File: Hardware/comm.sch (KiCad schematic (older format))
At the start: 13 parts, among them P301 PROGRAM, P302 OUTPUT, P303 INPUT, P304 BOOT, SW301 SW_Push

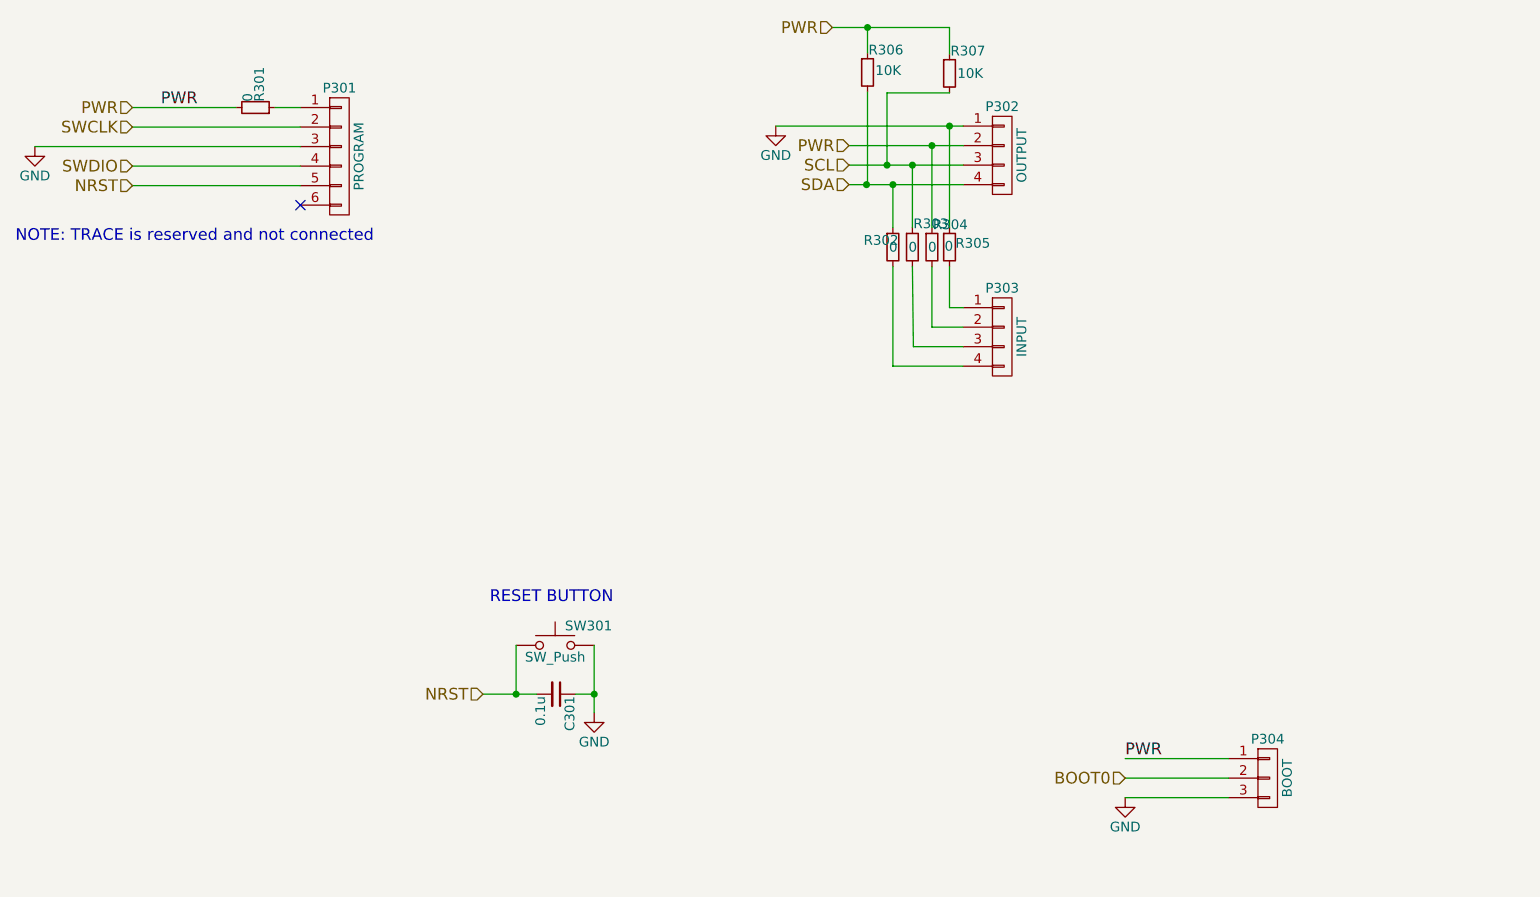
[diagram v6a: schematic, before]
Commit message: converted VCCIO to 3V3 and added 1x2 power and gnd
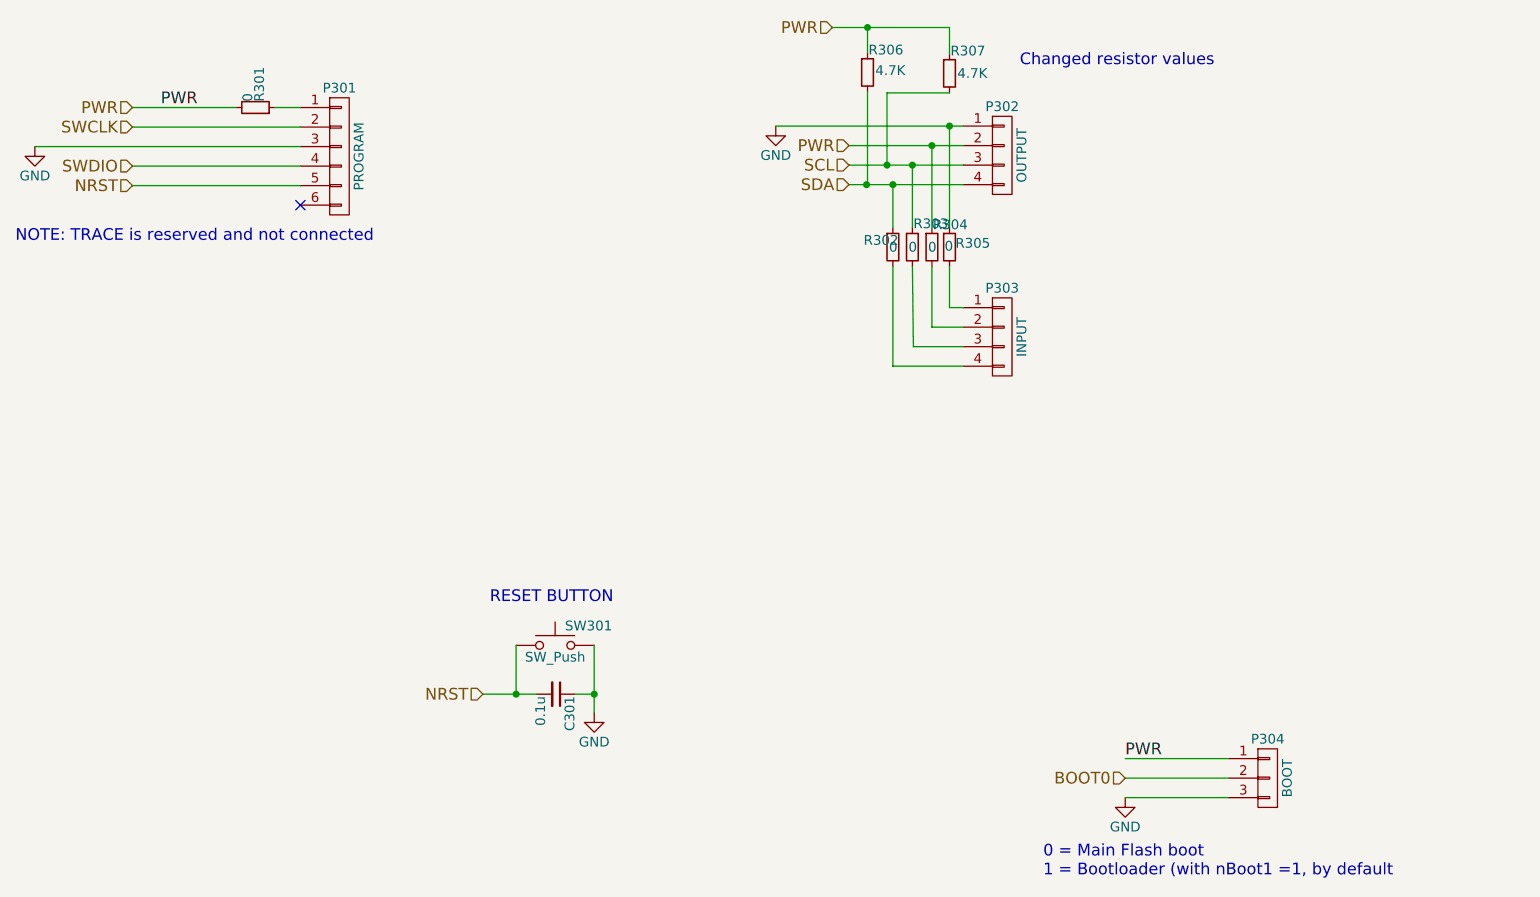
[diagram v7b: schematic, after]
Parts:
- R306, R307: value 10K -> 4.7K
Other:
- note added: "0 = Main Flash boot\n1 = Bootloader (with nBoot1 =1, by default"
- note added: "Changed resistor values"
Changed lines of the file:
@@
 SWCLK
 $Comp
-L GND #PWR020
+L GND #PWR021
 U 1 1 58DF9E37
 P 2955 1245
-F 0 "#PWR020" H 2955 995 50  0001 C CNN
+F 0 "#PWR021" H 2955 995 50  0001 C CNN
 F 1 "GND" H 2955 1095 50  0000 C CNN
 F 2 "" H 2955 1245 50  0000 C CNN
@@
 PWR
 $Comp
-L GND #PWR021
+L GND #PWR022
 U 1 1 58E10BA0
 P 6750 1140
-F 0 "#PWR021" H 6750 890 50  0001 C CNN
+F 0 "#PWR022" H 6750 890 50  0001 C CNN
 F 1 "GND" H 6750 990 50  0000 C CNN
 F 2 "" H 6750 1140 50  0000 C CNN
@@
 $EndComp
 $Comp
-L GND #PWR022
+L GND #PWR023
 U 1 1 58E1344F
 P 5820 4145
-F 0 "#PWR022" H 5820 3895 50  0001 C CNN
+F 0 "#PWR023" H 5820 3895 50  0001 C CNN
 F 1 "GND" H 5820 3995 50  0000 C CNN
 F 2 "" H 5820 4145 50  0000 C CNN
@@
 PWR
 $Comp
-L GND #PWR023
+L GND #PWR024
 U 1 1 58E18682
 P 8540 4580
-F 0 "#PWR023" H 8540 4330 50  0001 C CNN
+F 0 "#PWR024" H 8540 4330 50  0001 C CNN
 F 1 "GND" H 8540 4430 50  0000 C CNN
 F 2 "" H 8540 4580 50  0000 C CNN
@@
 P 7220 865
 F 0 "R306" H 7225 980 50  0000 L CNN
-F 1 "10K" H 7260 875 50  0000 L CNN
+F 1 "4.7K" H 7260 875 50  0000 L CNN
 F 2 "Resistors_SMD:R_0805" H 7220 865 50  0001 C CNN
 F 3 "" H 7220 865 50  0000 C CNN
@@
 P 7640 870
 F 0 "R307" H 7645 985 50  0000 L CNN
-F 1 "10K" H 7680 870 50  0000 L CNN
+F 1 "4.7K" H 7680 870 50  0000 L CNN
 F 2 "Resistors_SMD:R_0805" H 7640 870 50  0001 C CNN
 F 3 "" H 7640 870 50  0000 C CNN
@@
 	7320 970  7320 1340
 Connection ~ 7320 1340
+Text Notes 8120 4990 0    60   ~ 0
+0 = Main Flash boot\n1 = Bootloader (with nBoot1 =1, by default
+Text Notes 8000 840  0    60   ~ 0
+Changed resistor values
 $EndSCHEMATC
